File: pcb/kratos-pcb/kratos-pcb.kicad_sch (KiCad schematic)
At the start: 1 part, among them U1 ESP32-DEVKIT-V1

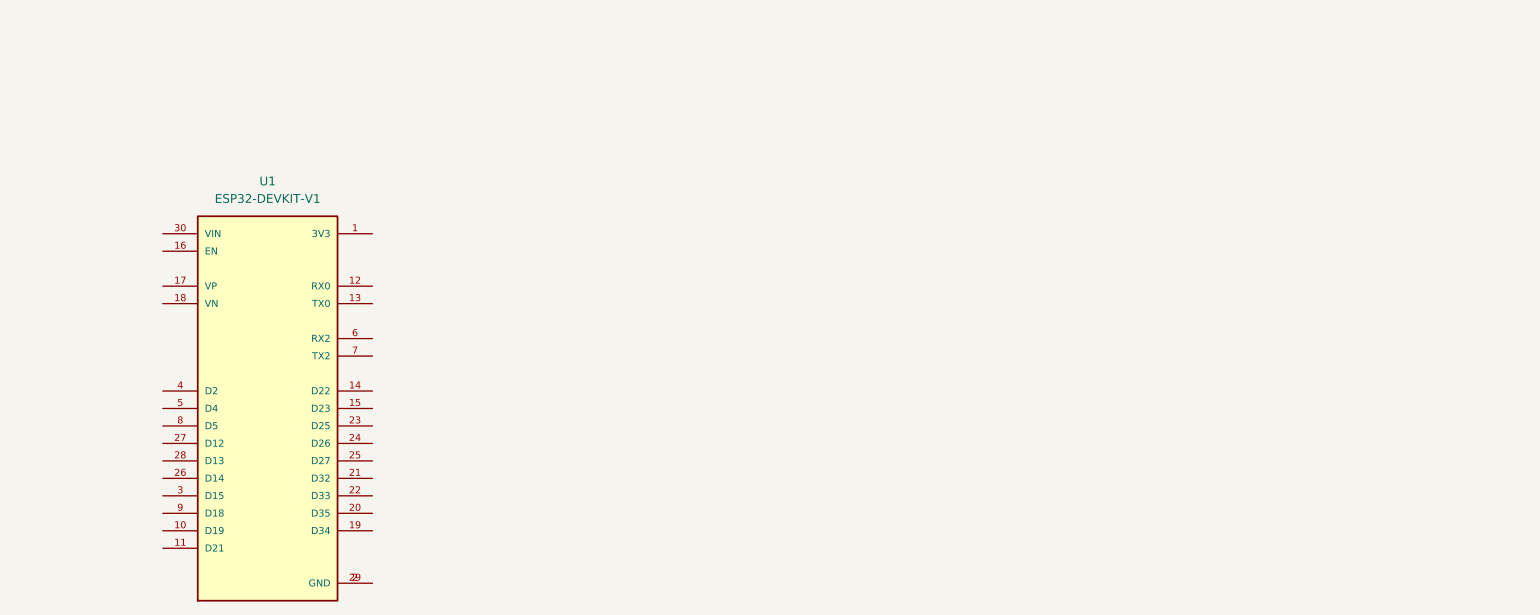
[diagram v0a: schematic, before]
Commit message: ### added
- pcb schematic
- controller
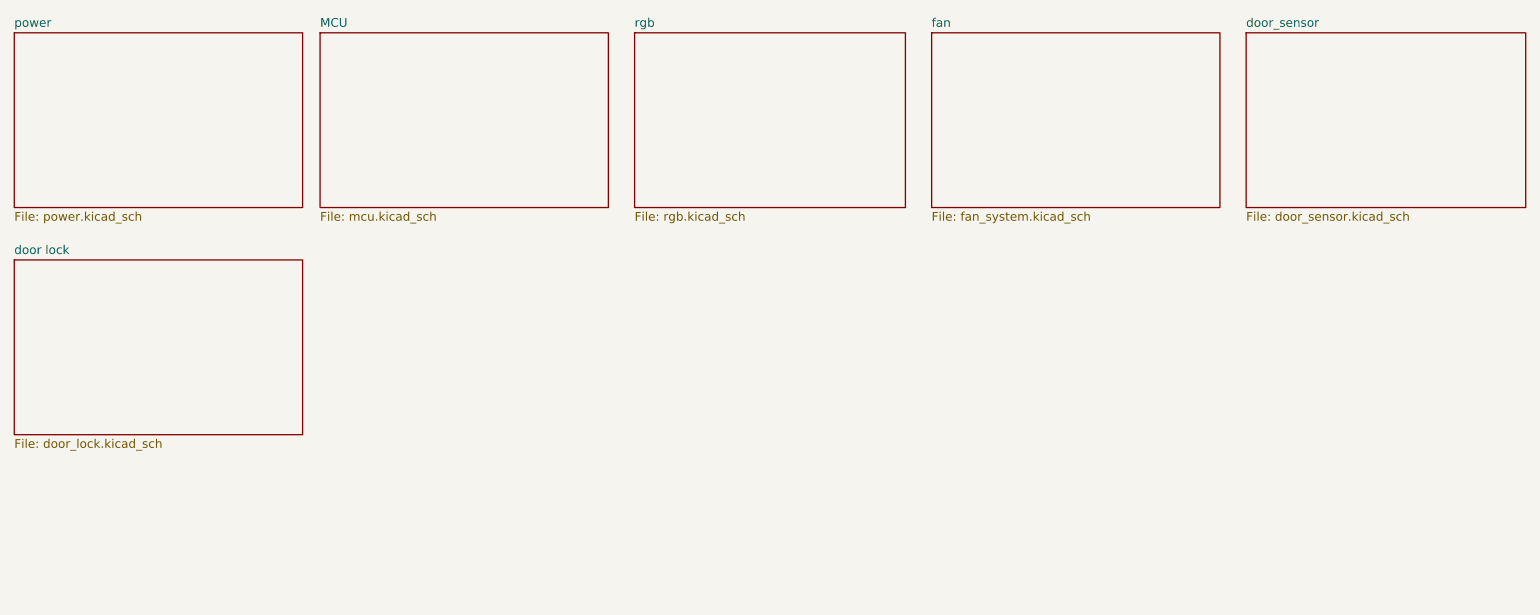
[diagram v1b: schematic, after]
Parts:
- removed U1: ESP32-DEVKIT-V1, footprints:MODULE_ESP32_DEVKIT_V1, symbol ESP32-DEVKIT-V1:ESP32-DEVKIT-V1
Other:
- added sheet MCU (mcu.kicad_sch)
- added sheet door lock (door_lock.kicad_sch)
- added sheet door_sensor (door_sensor.kicad_sch)
- added sheet fan (fan_system.kicad_sch)
- added sheet power (power.kicad_sch)
- added sheet rgb (rgb.kicad_sch)
- company: (none) -> Vortex
- title: (none) -> Project Kratos PCB
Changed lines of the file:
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@@
 (kicad_sch (version 20230121) (generator eeschema)
   (paper "A4")
-  (symbol (lib_id "ESP32-DEVKIT-V1:ESP32-DEVKIT-V1") (at 55.88 76.2 0) (unit 1)
-    (in_bom yes) (on_board yes) (dnp no) (fields_autoplaced)
-    (property "Reference" "U1" (at 55.88 43.18 0)
-      (effects (font (size 1.27 1.27)))
+  (title_block
+    (title "Project Kratos PCB")
+    (company "Vortex")
+  )
+  (sheet (at 19.05 21.59) (size 41.91 25.4) (fields_autoplaced)
+    (stroke (width 0.1524) (type solid))
+    (fill (color 0 0 0 0.0000))
+    (property "Sheetname" "power" (at 19.05 20.8784 0)
+      (effects (font (size 1.27 1.27)) (justify left bottom))
     )
-    (property "Value" "ESP32-DEVKIT-V1" (at 55.88 45.72 0)
-      (effects (font (size 1.27 1.27)))
+    (property "Sheetfile" "power.kicad_sch" (at 19.05 47.5746 0)
+      (effects (font (size 1.27 1.27)) (justify left top))
     )
-    (property "Footprint" "footprints:MODULE_ESP32_DEVKIT_V1" (at 55.88 76.2 0)
-      (effects (font (size 1.27 1.27)) (justify bottom) hide)
+    (instances
+      (project "kratos-pcb"
+        (path "/12f1b997-8c5f-4ef7-b036-7873ddaba48e" (page "2"))
+      )
     )
-    (property "Datasheet" "" (at 55.88 76.2 0)
+  )
+  (sheet (at 109.22 21.59) (size 39.37 25.4) (fields_autoplaced)
+    (stroke (width 0.1524) (type solid))
+    (fill (color 0 0 0 0.0000))
+    (property "Sheetname" "rgb" (at 109.22 20.8784 0)
+      (effects (font (size 1.27 1.27)) (justify left bottom))
+    )
+    (property "Sheetfile" "rgb.kicad_sch" (at 109.22 47.5746 0)
+      (effects (font (size 1.27 1.27)) (justify left top))
+    )
+    (property "Field2" "" (at 109.22 21.59 0)
       (effects (font (size 1.27 1.27)) hide)
     )
-    (property "STANDARD" "Manufacturer Recommendations" (at 55.88 76.2 0)
-      (effects (font (size 1.27 1.27)) (justify bottom) hide)
-    )
-    (property "MAXIMUM_PACKAGE_HEIGHT" "6.8 mm" (at 55.88 76.2 0)
-      (effects (font (size 1.27 1.27)) (justify bottom) hide)
-    )
-    (property "MANUFACTURER" "DOIT" (at 55.88 76.2 0)
-      (effects (font (size 1.27 1.27)) (justify bottom) hide)
-    )
-    (property "PARTREV" "N/A" (at 55.88 76.2 0)
-      (effects (font (size 1.27 1.27)) (justify bottom) hide)
-    )
-    (pin "4")
-    (pin "17")
-    (pin "12")
-    (pin "18")
-    (pin "28")
-    (pin "30")
-    (pin "13")
-    (pin "2")
-    (pin "9")
-    (pin "5")
-    (pin "8")
-    (pin "19")
-    (pin "24")
-    (pin "20")
-    (pin "25")
-    (pin "23")
-    (pin "11")
-    (pin "27")
-    (pin "7")
-    (pin "6")
-    (pin "15")
-    (pin "14")
-    (pin "3")
-    (pin "29")
-    (pin "1")
-    (pin "10")
-    (pin "26")
-    (pin "16")
-    (pin "22")
-    (pin "21")
     (instances
       (project "kratos-pcb"
-        (path "/12f1b997-8c5f-4ef7-b036-7873ddaba48e"
-          (reference "U1") (unit 1)
-        )
+        (path "/12f1b997-8c5f-4ef7-b036-7873ddaba48e" (page "4"))
       )
     )
+  )
+  (sheet (at 152.4 21.59) (size 41.91 25.4) (fields_autoplaced)
+    (stroke (width 0.1524) (type solid))
+    (fill (color 0 0 0 0.0000))
+    (property "Sheetname" "fan" (at 152.4 20.8784 0)
+      (effects (font (size 1.27 1.27)) (justify left bottom))
+    )
+    (property "Sheetfile" "fan_system.kicad_sch" (at 152.4 47.5746 0)
+      (effects (font (size 1.27 1.27)) (justify left top))
+    )
+    (instances
+      (project "kratos-pcb"
+        (path "/12f1b997-8c5f-4ef7-b036-7873ddaba48e" (page "5"))
+      )
+    )
+  )
+  (sheet (at 198.12 21.59) (size 40.64 25.4) (fields_autoplaced)
+    (stroke (width 0.1524) (type solid))
+    (fill (color 0 0 0 0.0000))
+    (property "Sheetname" "door_sensor" (at 198.12 20.8784 0)
+      (effects (font (size 1.27 1.27)) (justify left bottom))
+    )
+    (property "Sheetfile" "door_sensor.kicad_sch" (at 198.12 47.5746 0)
+      (effects (font (size 1.27 1.27)) (justify left top))
+    )
+    (instances
+      (project "kratos-pcb"
+        (path "/12f1b997-8c5f-4ef7-b036-7873ddaba48e" (page "6"))
+      )
+    )
+  )
+  (sheet (at 63.5 21.59) (size 41.91 25.4) (fields_autoplaced)
+    (stroke (width 0.1524) (type solid))
+    (fill (color 0 0 0 0.0000))
+    (property "Sheetname" "MCU" (at 63.5 20.8784 0)
+      (effects (font (size 1.27 1.27)) (justify left bottom))
+    )
+    (property "Sheetfile" "mcu.kicad_sch" (at 63.5 47.5746 0)
+      (effects (font (size 1.27 1.27)) (justify left top))
+    )
+    (instances
+      (project "kratos-pcb"
+        (path "/12f1b997-8c5f-4ef7-b036-7873ddaba48e" (page "3"))
+      )
+    )
+  )
+  (sheet (at 19.05 54.61) (size 41.91 25.4) (fields_autoplaced)
+    (stroke (width 0.1524) (type solid))
+    (fill (color 0 0 0 0.0000))
+    (property "Sheetname" "door lock" (at 19.05 53.8984 0)
+      (effects (font (size 1.27 1.27)) (justify left bottom))
+    )
+    (property "Sheetfile" "door_lock.kicad_sch" (at 19.05 80.5946 0)
+      (effects (font (size 1.27 1.27)) (justify left top))
+    )
+    (instances
+      (project "kratos-pcb"
+        (path "/12f1b997-8c5f-4ef7-b036-7873ddaba48e" (page "7"))
+      )
+    )

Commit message: ### added
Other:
- added sheet Shift Register (ioexpantion.kicad_sch)
- added sheet dht22 (dht22.kicad_sch)
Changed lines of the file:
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@@
+    )
+  )
+  (sheet (at 64.77 55.88) (size 41.91 22.86) (fields_autoplaced)
+    (stroke (width 0.1524) (type solid))
+    (fill (color 0 0 0 0.0000))
+    (property "Sheetname" "Shift Register" (at 64.77 55.1684 0)
+      (effects (font (size 1.27 1.27)) (justify left bottom))
+    )
+    (property "Sheetfile" "ioexpantion.kicad_sch" (at 64.77 79.3246 0)
+      (effects (font (size 1.27 1.27)) (justify left top))
+    )
+    (instances
+      (project "kratos-pcb"
+        (path "/12f1b997-8c5f-4ef7-b036-7873ddaba48e" (page "8"))
+      )
+    )
+  )
+  (sheet (at 109.22 55.88) (size 40.64 21.59) (fields_autoplaced)
+    (stroke (width 0.1524) (type solid))
+    (fill (color 0 0 0 0.0000))
+    (property "Sheetname" "dht22" (at 109.22 55.1684 0)
+      (effects (font (size 1.27 1.27)) (justify left bottom))
+    )
+    (property "Sheetfile" "dht22.kicad_sch" (at 109.22 78.0546 0)
+      (effects (font (size 1.27 1.27)) (justify left top))
+    )
+    (instances
+      (project "kratos-pcb"
+        (path "/12f1b997-8c5f-4ef7-b036-7873ddaba48e" (page "9"))
+      )
     )
   )

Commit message: ### update     - kicad schematic
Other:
- sheet Shift Register renamed EXPANSION DRIVERS
- sheet dht22 renamed DHT22-SENSOR
- sheet door lock renamed LOCKER
- sheet door_sensor renamed SDOOR
- sheet fan renamed FAN
- sheet power renamed POWER SUPPLY
- removed sheet rgb
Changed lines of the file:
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@@
     (stroke (width 0.1524) (type solid))
     (fill (color 0 0 0 0.0000))
-    (property "Sheetname" "power" (at 19.05 20.8784 0)
+    (property "Sheetname" "POWER SUPPLY" (at 19.05 20.8784 0)
       (effects (font (size 1.27 1.27)) (justify left bottom))
     )
@@
     )
   )
-  (sheet (at 109.22 21.59) (size 39.37 25.4) (fields_autoplaced)
-    (stroke (width 0.1524) (type solid))
-    (fill (color 0 0 0 0.0000))
-    (property "Sheetname" "rgb" (at 109.22 20.8784 0)
-      (effects (font (size 1.27 1.27)) (justify left bottom))
-    )
-    (property "Sheetfile" "rgb.kicad_sch" (at 109.22 47.5746 0)
-      (effects (font (size 1.27 1.27)) (justify left top))
-    )
-    (property "Field2" "" (at 109.22 21.59 0)
-      (effects (font (size 1.27 1.27)) hide)
-    )
-    (instances
-      (project "kratos-pcb"
-        (path "/12f1b997-8c5f-4ef7-b036-7873ddaba48e" (page "4"))
-      )
-    )
-  )
   (sheet (at 152.4 21.59) (size 41.91 25.4) (fields_autoplaced)
     (stroke (width 0.1524) (type solid))
     (fill (color 0 0 0 0.0000))
-    (property "Sheetname" "fan" (at 152.4 20.8784 0)
+    (property "Sheetname" "FAN" (at 152.4 20.8784 0)
       (effects (font (size 1.27 1.27)) (justify left bottom))
     )
@@
     (stroke (width 0.1524) (type solid))
     (fill (color 0 0 0 0.0000))
-    (property "Sheetname" "door_sensor" (at 198.12 20.8784 0)
+    (property "Sheetname" "SDOOR" (at 198.12 20.8784 0)
       (effects (font (size 1.27 1.27)) (justify left bottom))
     )
@@
     )
   )
-  (sheet (at 64.77 55.88) (size 41.91 22.86) (fields_autoplaced)
+  (sheet (at 106.68 21.59) (size 43.18 25.4) (fields_autoplaced)
     (stroke (width 0.1524) (type solid))
     (fill (color 0 0 0 0.0000))
-    (property "Sheetname" "Shift Register" (at 64.77 55.1684 0)
+    (property "Sheetname" "EXPANSION DRIVERS" (at 106.68 20.8784 0)
       (effects (font (size 1.27 1.27)) (justify left bottom))
     )
-    (property "Sheetfile" "ioexpantion.kicad_sch" (at 64.77 79.3246 0)
+    (property "Sheetfile" "ioexpantion.kicad_sch" (at 106.68 47.5746 0)
       (effects (font (size 1.27 1.27)) (justify left top))
     )
@@
     )
   )
-  (sheet (at 109.22 55.88) (size 40.64 21.59) (fields_autoplaced)
+  (sheet (at 63.5 54.61) (size 40.64 25.4) (fields_autoplaced)
     (stroke (width 0.1524) (type solid))
     (fill (color 0 0 0 0.0000))
-    (property "Sheetname" "dht22" (at 109.22 55.1684 0)
+    (property "Sheetname" "DHT22-SENSOR" (at 63.5 53.8984 0)
       (effects (font (size 1.27 1.27)) (justify left bottom))
     )
-    (property "Sheetfile" "dht22.kicad_sch" (at 109.22 78.0546 0)
+    (property "Sheetfile" "dht22.kicad_sch" (at 63.5 80.5946 0)
       (effects (font (size 1.27 1.27)) (justify left top))
     )
@@
     (stroke (width 0.1524) (type solid))
     (fill (color 0 0 0 0.0000))
-    (property "Sheetname" "door lock" (at 19.05 53.8984 0)
+    (property "Sheetname" "LOCKER" (at 19.05 53.8984 0)
       (effects (font (size 1.27 1.27)) (justify left bottom))
     )

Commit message: ### door sistem
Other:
- added sheet rfid (rfid.kicad_sch)
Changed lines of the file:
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@@
+    )
+  )
+  (sheet (at 106.68 54.61) (size 44.45 25.4) (fields_autoplaced)
+    (stroke (width 0.1524) (type solid))
+    (fill (color 0 0 0 0.0000))
+    (property "Sheetname" "rfid" (at 106.68 53.8984 0)
+      (effects (font (size 1.27 1.27)) (justify left bottom))
+    )
+    (property "Sheetfile" "rfid.kicad_sch" (at 106.68 80.5946 0)
+      (effects (font (size 1.27 1.27)) (justify left top))
+    )
+    (instances
+      (project "kratos-pcb"
+        (path "/12f1b997-8c5f-4ef7-b036-7873ddaba48e" (page "9"))
+      )
     )
   )
